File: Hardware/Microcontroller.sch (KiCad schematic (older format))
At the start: 21 parts, among them J1 UPDI, J2 UART, J3 NMEA, J4 Vin, Q1 S8050, U3 ATtiny1606-S, U4 L78M05ABDT-TR

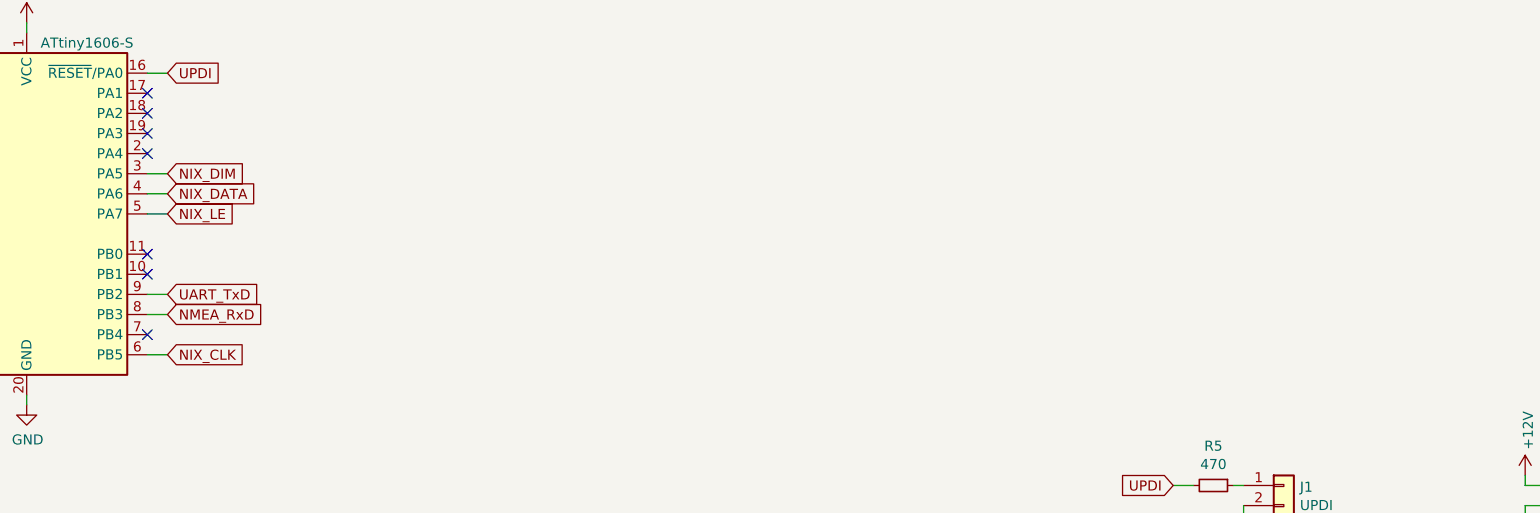
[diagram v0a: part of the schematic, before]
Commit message: Add timezone switch
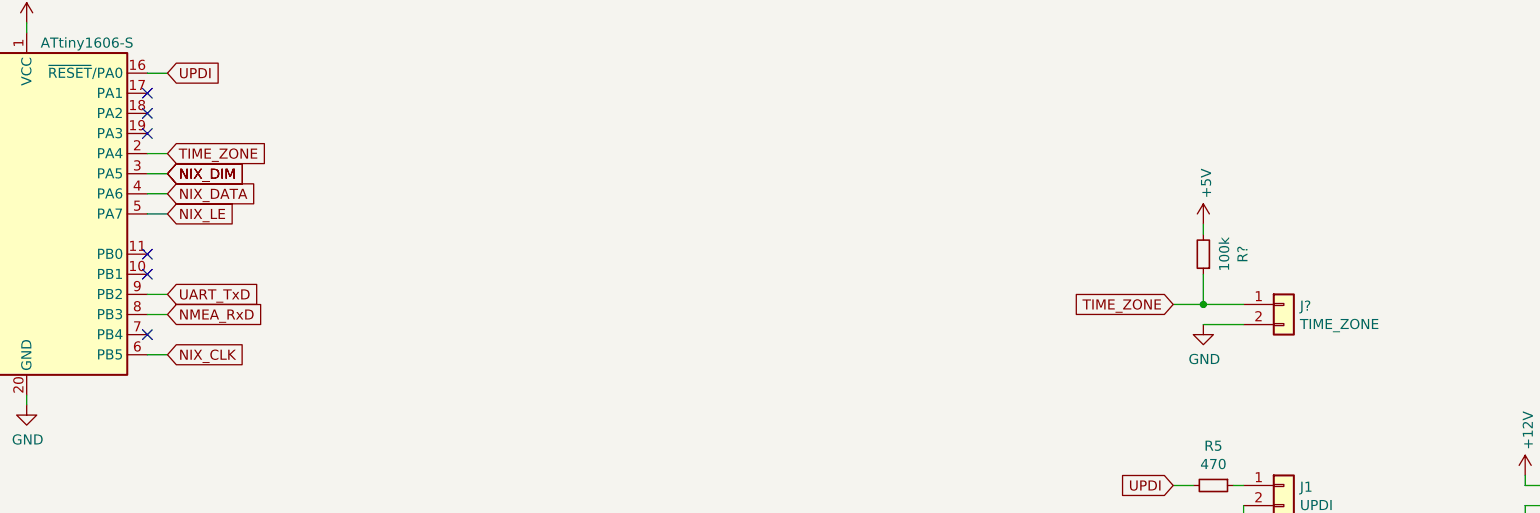
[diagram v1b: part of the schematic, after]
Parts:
- added J?: TIME_ZONE, Connector_PinHeader_2.54mm:PinHeader_1x02_P2.54mm_Vertical, symbol Connector_Generic:Conn_01x02
- added R?: 100k, Resistor_SMD:R_0603_1608Metric, symbol Device:R_Small
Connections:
- net +5V: now also R?.2
- net GND: now also J?.2 (Pin_2)
- net TIME_ZONE: now reaches U3.2 (PA4)
- net TIME_ZONE: now also J?.1 (Pin_1), R?.1
- no-connect marks 11 -> 10
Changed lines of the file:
@@
 $EndComp
 NoConn ~ 2750 2800
-NoConn ~ 2750 1900
 NoConn ~ 2750 1800
 NoConn ~ 1550 2700
@@
 Wire Wire Line
 	9750 4500 9950 4500
+Text GLabel 2850 2000 2    50   Input ~ 0
+NIX_DIM
+Text GLabel 2850 1900 2    50   Input ~ 0
+TIME_ZONE
+Wire Wire Line
+	2750 1900 2850 1900
+$Comp
+L Connector_Generic:Conn_01x02 J?
+U 1 1 5FB947CD
+P 8400 2650
+AR Path="/5F57C9A4/5FB947CD" Ref="J?"  Part="1"
+AR Path="/5F63C067/5FB947CD" Ref="J?"  Part="1"
+F 0 "J?" H 8480 2642 50  0000 L CNN
+F 1 "TIME_ZONE" H 8480 2551 50  0000 L CNN
+F 2 "Connector_PinHeader_2.54mm:PinHeader_1x02_P2.54mm_Vertical" H 8400 2650 50  0001 C CNN
+F 3 "~" H 8400 2650 50  0001 C CNN
+	1    8400 2650
+	1    0    0    -1
+$EndComp
+$Comp
+L power:GND #PWR?
+U 1 1 5FB947E7
+P 8000 2750
+AR Path="/5F8C807E/5FB947E7" Ref="#PWR?"  Part="1"
+AR Path="/5FB947E7" Ref="#PWR?"  Part="1"
+AR Path="/5F57C9A4/5FB947E7" Ref="#PWR?"  Part="1"
+AR Path="/5F57DBA0/5FB947E7" Ref="#PWR?"  Part="1"
+AR Path="/5F63C067/5FB947E7" Ref="#PWR?"  Part="1"
+F 0 "#PWR?" H 8000 2500 50  0001 C CNN
+F 1 "GND" H 8005 2577 50  0000 C CNN
+F 2 "" H 8000 2750 50  0001 C CNN
+F 3 "" H 8000 2750 50  0001 C CNN
+	1    8000 2750
+	1    0    0    -1
+$EndComp
+Wire Wire Line
+	8200 2750 8000 2750
+$Comp
+L Device:R_Small R?
+U 1 1 5FB947F3
+P 8000 2400
+AR Path="/5F57C9A4/5FB947F3" Ref="R?"  Part="1"
+AR Path="/5F63C067/5FB947F3" Ref="R?"  Part="1"
+F 0 "R?" V 7804 2400 50  0000 C CNN
+F 1 "100k" V 7895 2400 50  0000 C CNN
+F 2 "Resistor_SMD:R_0603_1608Metric" H 8000 2400 50  0001 C CNN
+F 3 "~" H 8000 2400 50  0001 C CNN
+	1    8000 2400
+	-1   0    0    1
+$EndComp
+Text GLabel 7850 2650 0    50   Input ~ 0
+TIME_ZONE
+Wire Wire Line
+	7850 2650 8000 2650
+Wire Wire Line
+	8000 2500 8000 2650
+Connection ~ 8000 2650
+Wire Wire Line
+	8000 2650 8200 2650
+$Comp
+L power:+5V #PWR?
+U 1 1 5FB9E23E
+P 8000 2250
+AR Path="/5F8C807E/5FB9E23E" Ref="#PWR?"  Part="1"
+AR Path="/5FB9E23E" Ref="#PWR?"  Part="1"
+AR Path="/5F57C9A4/5FB9E23E" Ref="#PWR?"  Part="1"
+AR Path="/5F57DBA0/5FB9E23E" Ref="#PWR?"  Part="1"
+AR Path="/5F63C067/5FB9E23E" Ref="#PWR?"  Part="1"
+AR Path="/5F645C82/5FB9E23E" Ref="#PWR?"  Part="1"
+F 0 "#PWR?" H 8000 2100 50  0001 C CNN
+F 1 "+5V" V 8015 2378 50  0000 L CNN
+F 2 "" H 8000 2250 50  0001 C CNN
+F 3 "" H 8000 2250 50  0001 C CNN
+	1    8000 2250
+	1    0    0    -1
+$EndComp
+Wire Wire Line
+	8000 2300 8000 2250
 $EndSCHEMATC

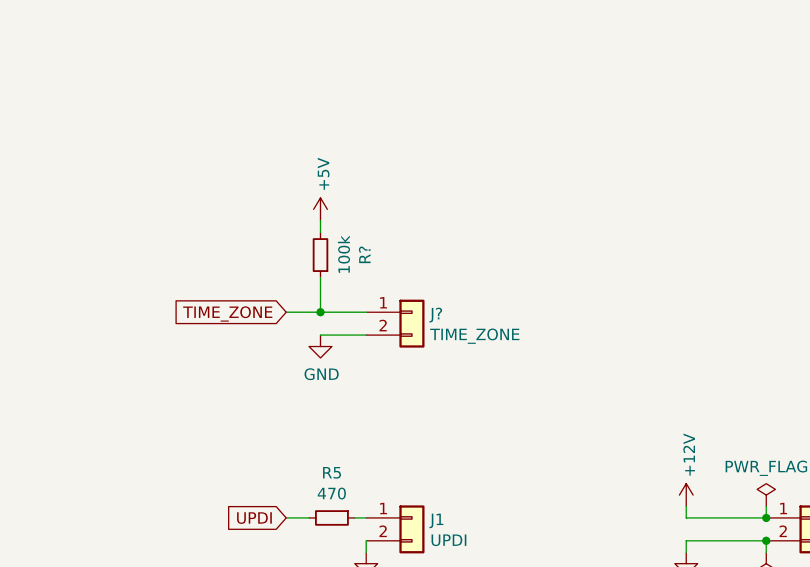
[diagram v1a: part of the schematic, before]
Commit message: Add forgotten file. Still belongs to v2
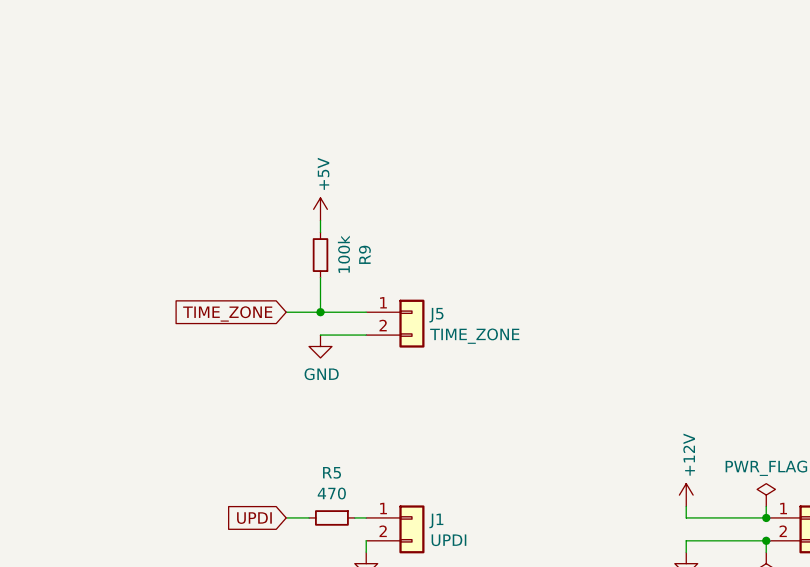
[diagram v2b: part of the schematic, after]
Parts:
- gave numbers to parts that had none: 2
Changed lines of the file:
@@
 	2750 1900 2850 1900
 $Comp
-L Connector_Generic:Conn_01x02 J?
+L Connector_Generic:Conn_01x02 J5
 U 1 1 5FB947CD
 P 8400 2650
-AR Path="/5F57C9A4/5FB947CD" Ref="J?"  Part="1"
+AR Path="/5F57C9A4/5FB947CD" Ref="J5"  Part="1"
 AR Path="/5F63C067/5FB947CD" Ref="J?"  Part="1"
-F 0 "J?" H 8480 2642 50  0000 L CNN
+F 0 "J5" H 8480 2642 50  0000 L CNN
 F 1 "TIME_ZONE" H 8480 2551 50  0000 L CNN
 F 2 "Connector_PinHeader_2.54mm:PinHeader_1x02_P2.54mm_Vertical" H 8400 2650 50  0001 C CNN
@@
 AR Path="/5F8C807E/5FB947E7" Ref="#PWR?"  Part="1"
 AR Path="/5FB947E7" Ref="#PWR?"  Part="1"
-AR Path="/5F57C9A4/5FB947E7" Ref="#PWR?"  Part="1"
+AR Path="/5F57C9A4/5FB947E7" Ref="#PWR0119"  Part="1"
 AR Path="/5F57DBA0/5FB947E7" Ref="#PWR?"  Part="1"
 AR Path="/5F63C067/5FB947E7" Ref="#PWR?"  Part="1"
-F 0 "#PWR?" H 8000 2500 50  0001 C CNN
+F 0 "#PWR0119" H 8000 2500 50  0001 C CNN
 F 1 "GND" H 8005 2577 50  0000 C CNN
 F 2 "" H 8000 2750 50  0001 C CNN
@@
 	8200 2750 8000 2750
 $Comp
-L Device:R_Small R?
+L Device:R_Small R9
 U 1 1 5FB947F3
 P 8000 2400
-AR Path="/5F57C9A4/5FB947F3" Ref="R?"  Part="1"
+AR Path="/5F57C9A4/5FB947F3" Ref="R9"  Part="1"
 AR Path="/5F63C067/5FB947F3" Ref="R?"  Part="1"
-F 0 "R?" V 7804 2400 50  0000 C CNN
+F 0 "R9" V 7804 2400 50  0000 C CNN
 F 1 "100k" V 7895 2400 50  0000 C CNN
 F 2 "Resistor_SMD:R_0603_1608Metric" H 8000 2400 50  0001 C CNN
@@
 AR Path="/5F8C807E/5FB9E23E" Ref="#PWR?"  Part="1"
 AR Path="/5FB9E23E" Ref="#PWR?"  Part="1"
-AR Path="/5F57C9A4/5FB9E23E" Ref="#PWR?"  Part="1"
+AR Path="/5F57C9A4/5FB9E23E" Ref="#PWR0120"  Part="1"
 AR Path="/5F57DBA0/5FB9E23E" Ref="#PWR?"  Part="1"
 AR Path="/5F63C067/5FB9E23E" Ref="#PWR?"  Part="1"
 AR Path="/5F645C82/5FB9E23E" Ref="#PWR?"  Part="1"
-F 0 "#PWR?" H 8000 2100 50  0001 C CNN
+F 0 "#PWR0120" H 8000 2100 50  0001 C CNN
 F 1 "+5V" V 8015 2378 50  0000 L CNN
 F 2 "" H 8000 2250 50  0001 C CNN
